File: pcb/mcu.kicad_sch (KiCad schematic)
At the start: 25 parts, among them J6 TC2030, U1 RP2040, U148 W25Q128JVS, Y1 ABM8AIG-12.000MHZ-12-2Z-T3

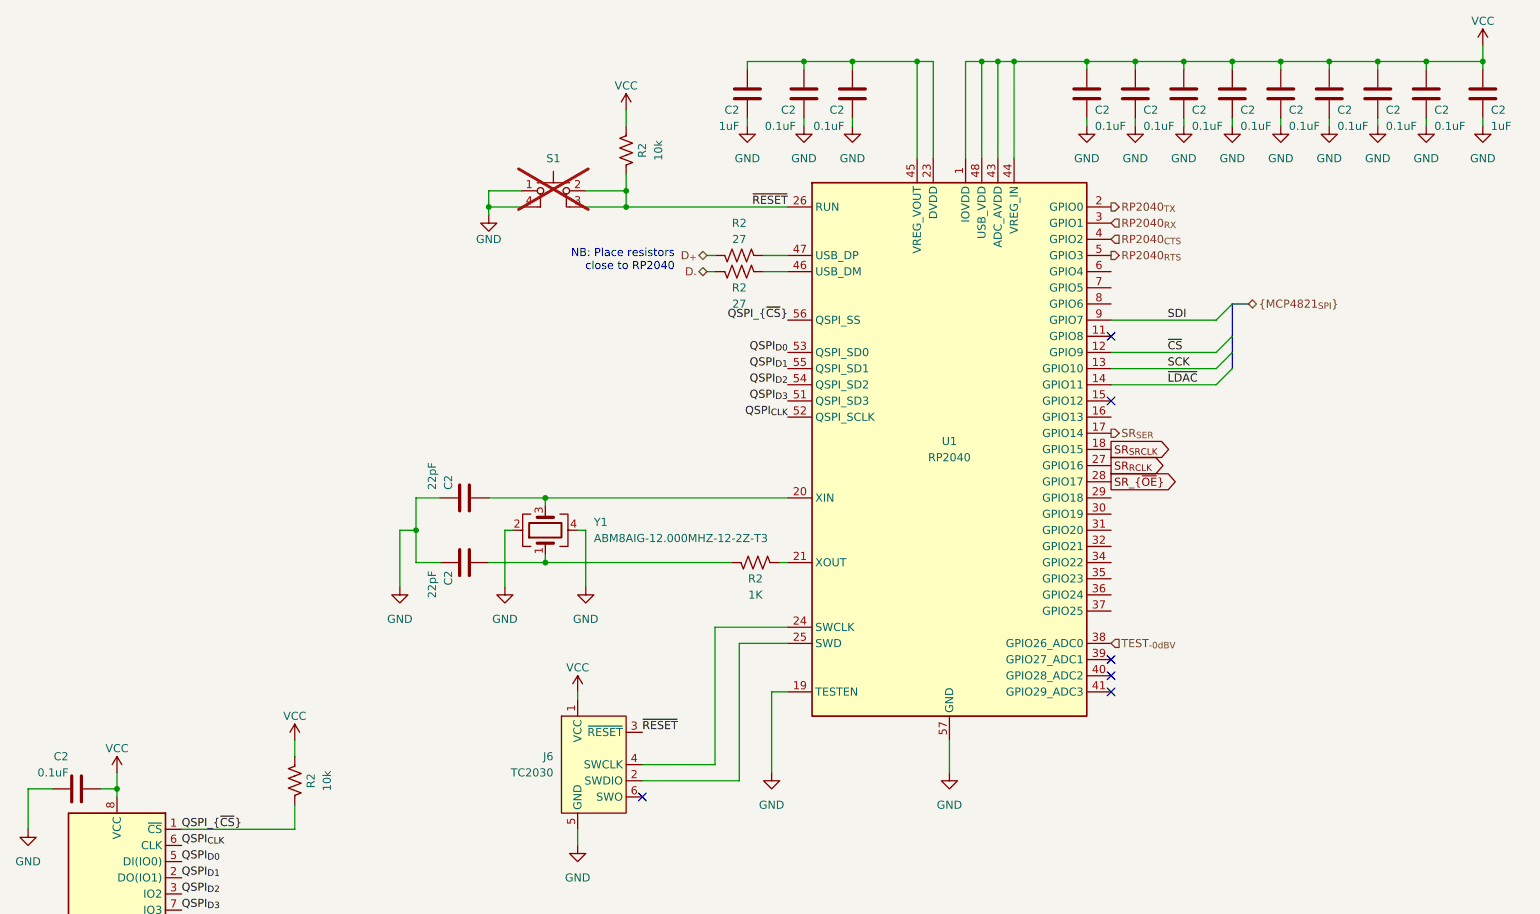
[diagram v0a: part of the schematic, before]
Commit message: Remove battery power option
- This device needs user IO
- Battery power means there would need to be a touch screen or wireless
  connection. Too complex.
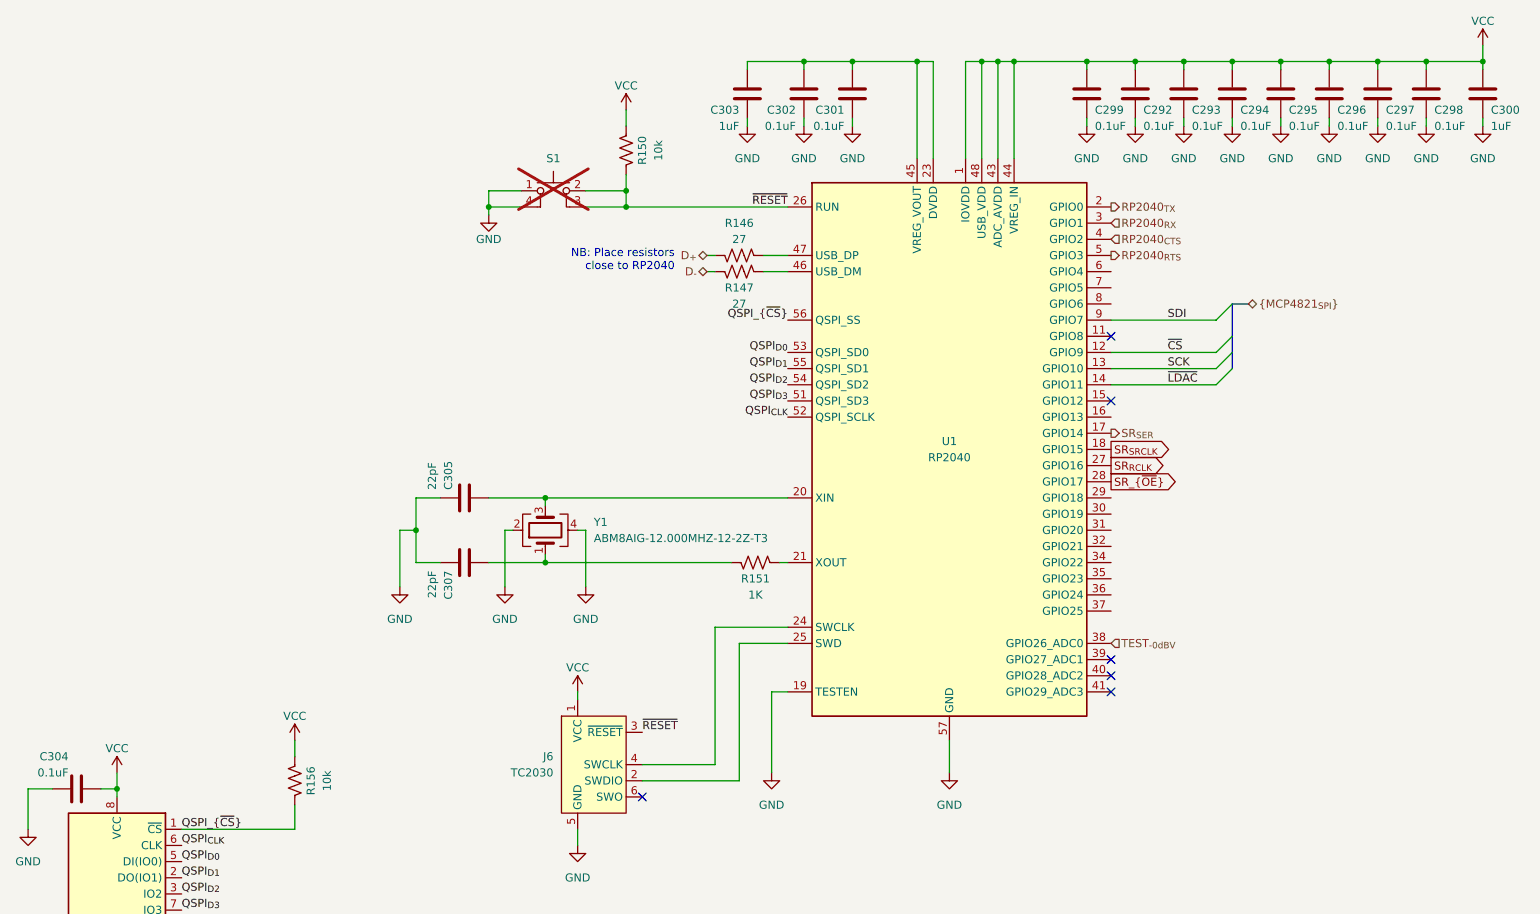
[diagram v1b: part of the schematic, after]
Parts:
- R146, R147, R150, R151, R156: renamed from R2; footprint (none) -> Resistor_SMD:R_0402_1005Metric
- S1: footprint (none) -> Button_Switch_THT:SW_PUSH_6mm_H4.3mm
- renumbered C2 to C292, C2 to C293, C2 to C294, C2 to C295, C2 to C296, C2 to C297, C2 to C298, C2 to C299, C2 to C300, C2 to C301, C2 to C302, C2 to C303, C2 to C304, C2 to C305, C2 to C307

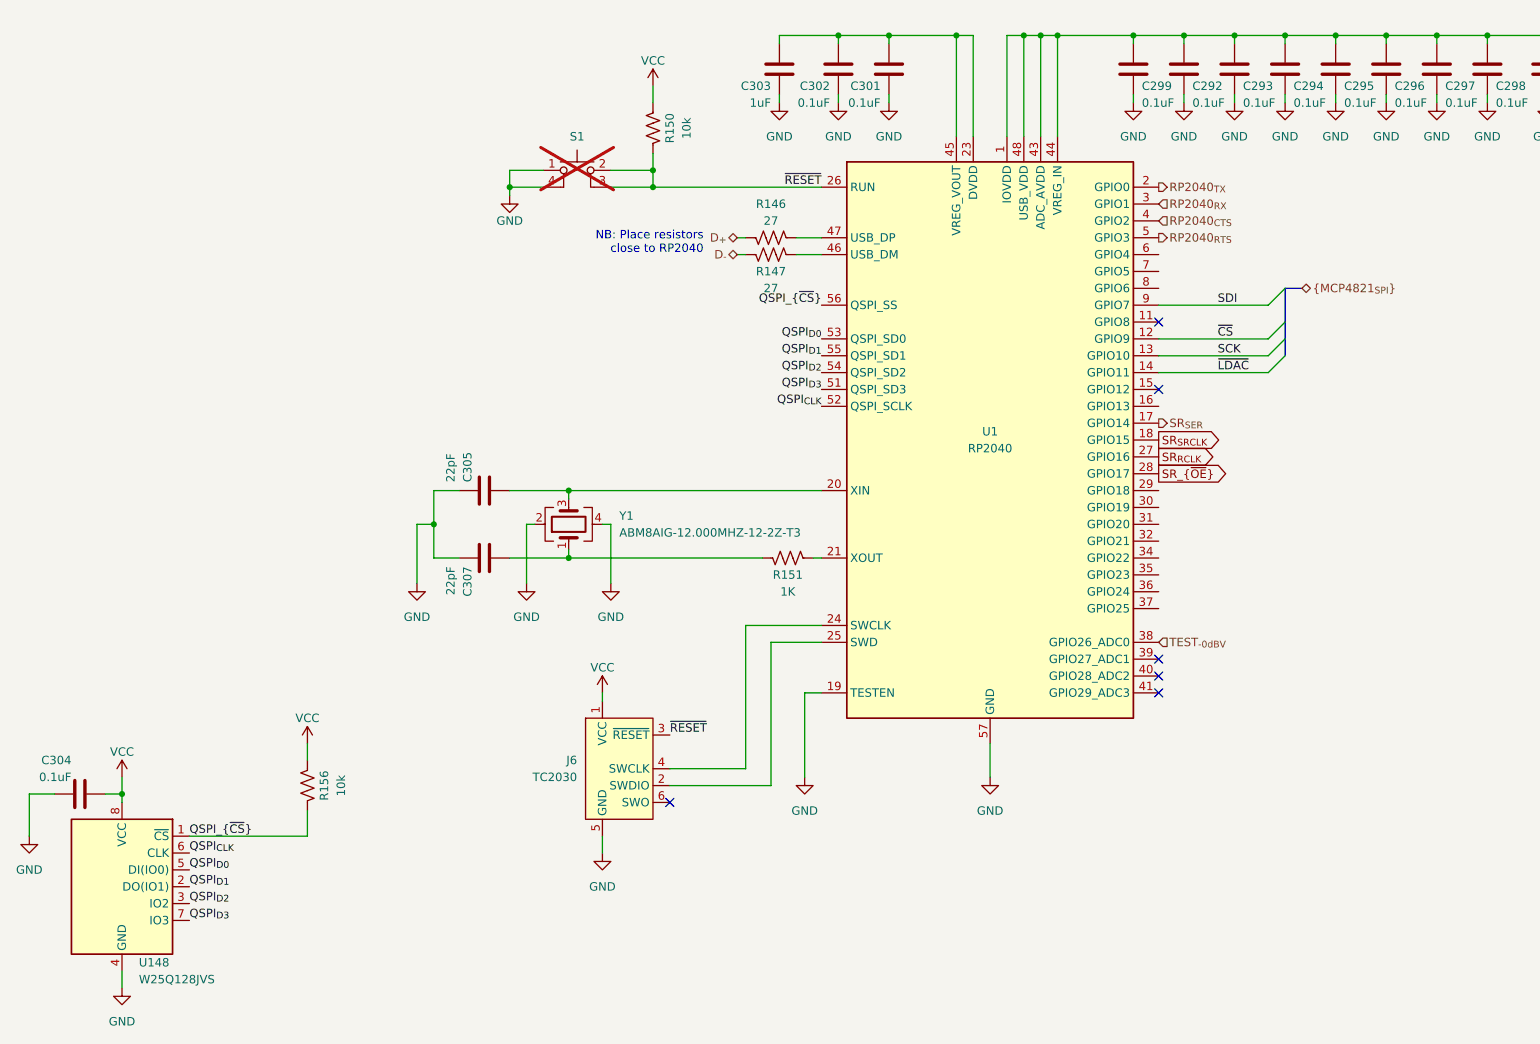
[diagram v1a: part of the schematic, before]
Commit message: Finished schematic, started routing
- There is a 8-channel motif that will need to be copied 16x on the
  board. I'm not sure the most efficient way to do this.
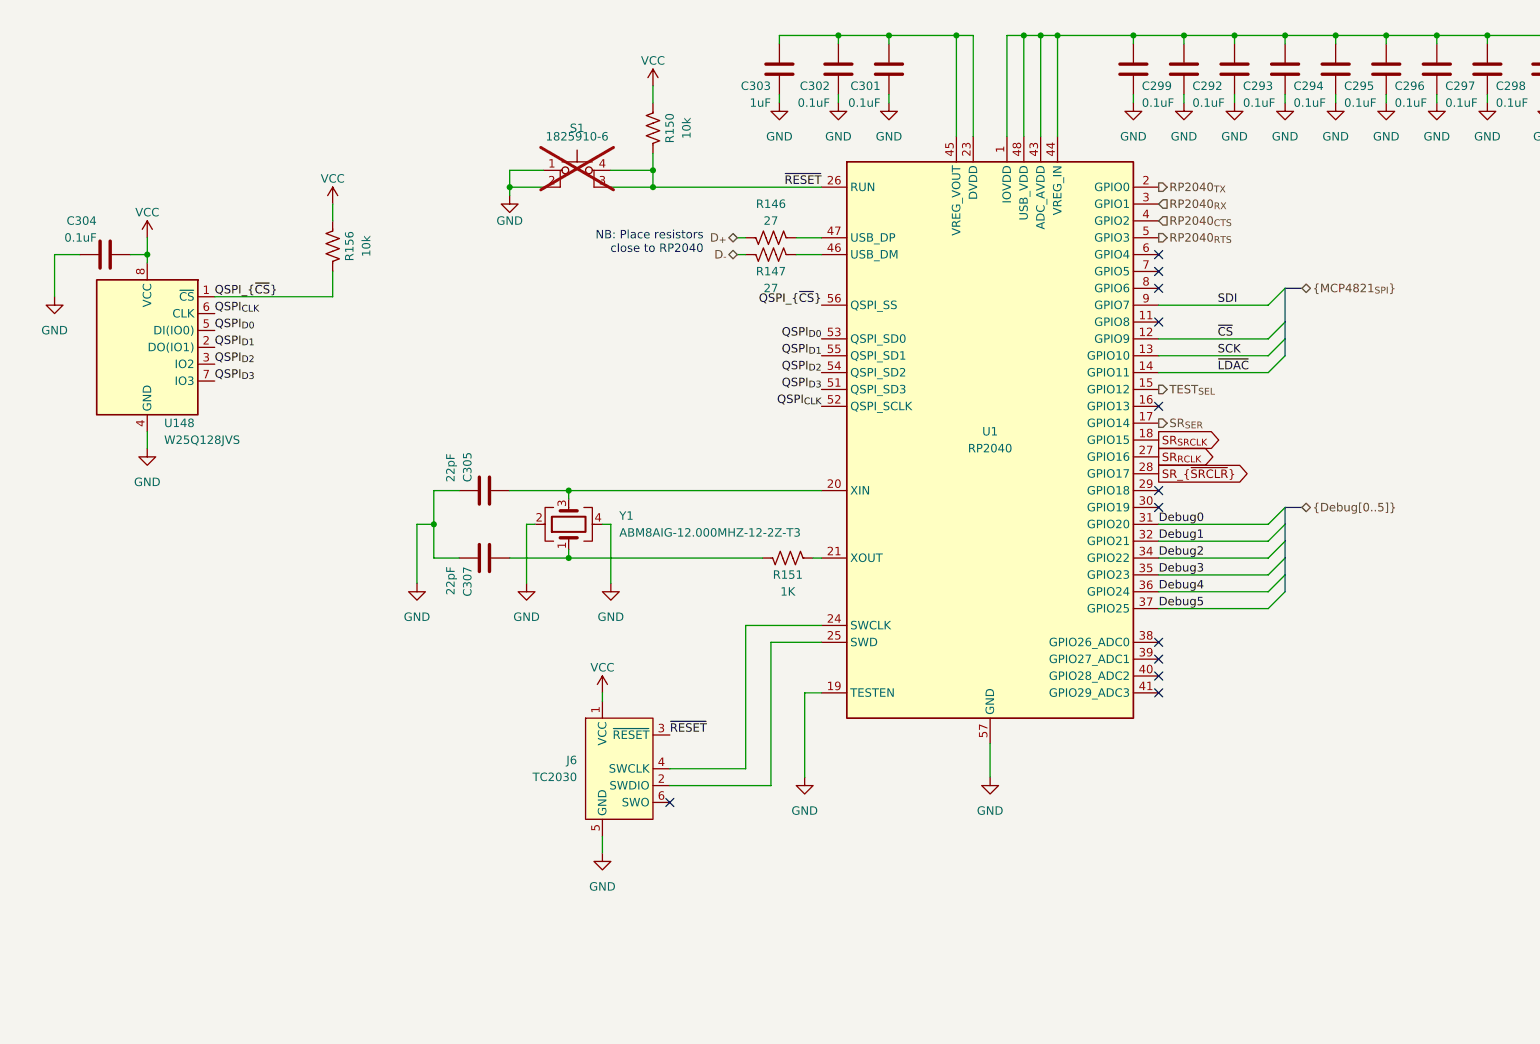
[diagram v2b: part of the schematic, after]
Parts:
- removed S1: ~, Button_Switch_THT:SW_PUSH_6mm_H4.3mm, symbol open-ephys:SW_TACT
- added S1: 1825910-6, Button_Switch_THT:SW_PUSH_6mm_H4.3mm, symbol Switch:SW_MEC_5E
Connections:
- net GND: now also S1.1, S1.2
- net ~{RESET}: now also S1.3 (K), S1.4 (A)
- net TEST_{SEL}: now reaches U1.15 (GPIO12)
- net Debug0: now reaches U1.31 (GPIO20)
- net Debug1: now reaches U1.32 (GPIO21)
- net Debug2: now reaches U1.34 (GPIO22)
- net Debug3: now reaches U1.35 (GPIO23)
- net Debug4: now reaches U1.36 (GPIO24)
- net Debug5: now reaches U1.37 (GPIO25)
- net SR_{~{OE}} renamed SR_{~{SRCLR}}
- net TEST_{-0dBV}: no longer names the net of U1.38 (GPIO26_ADC0)
- no-connect marks 6 -> 12
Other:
- moved on the sheet: C304, R156, U148

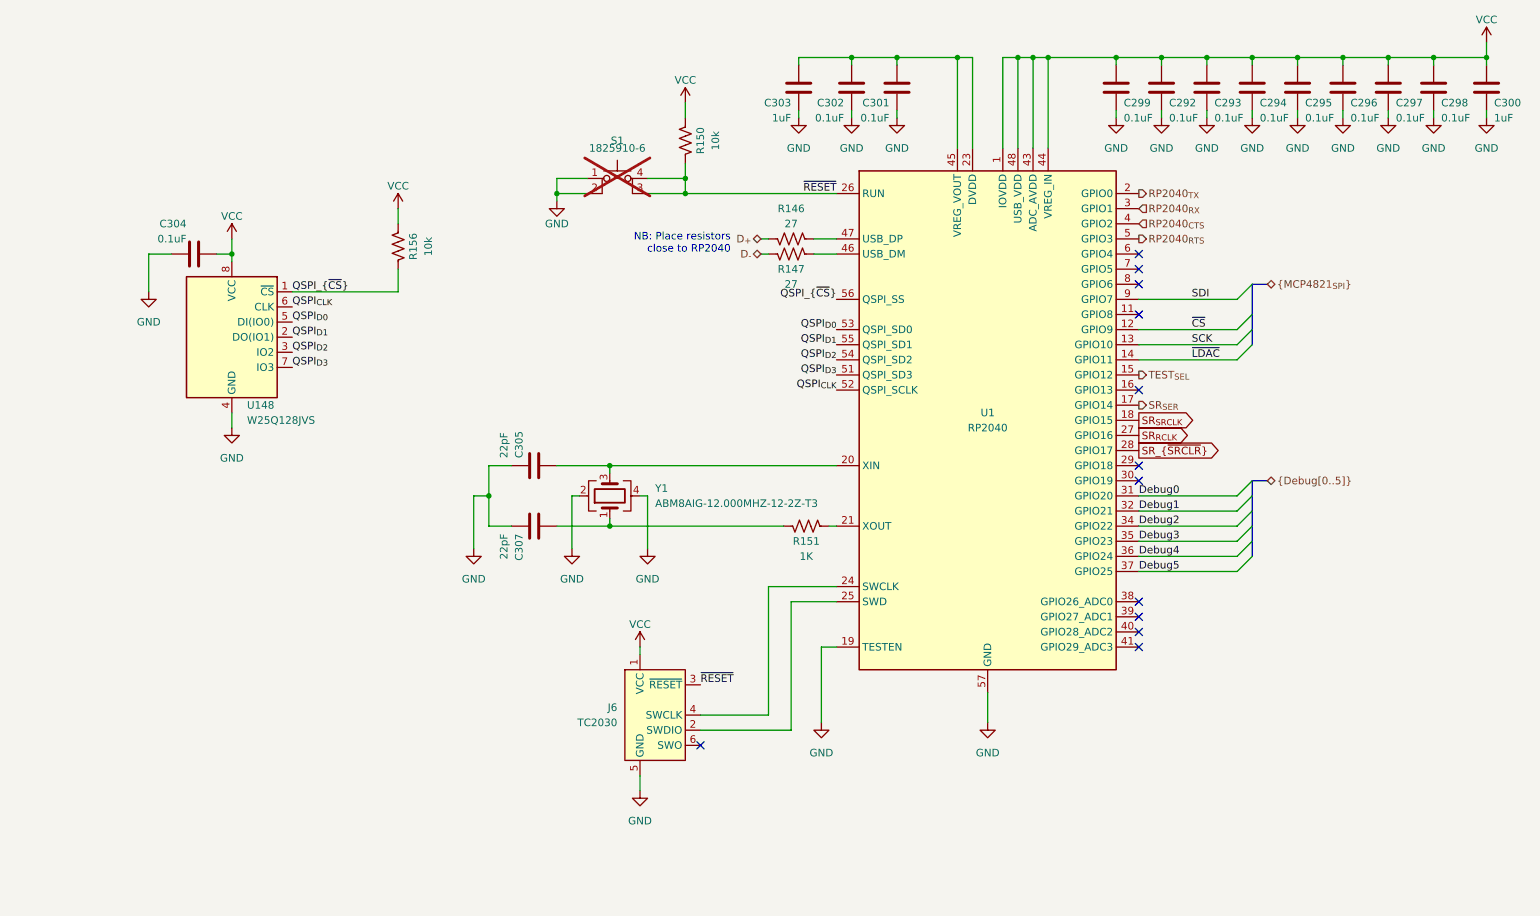
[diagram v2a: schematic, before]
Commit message: Motif is repeated
- some components are grouped by function
- components are roughly organized within groups
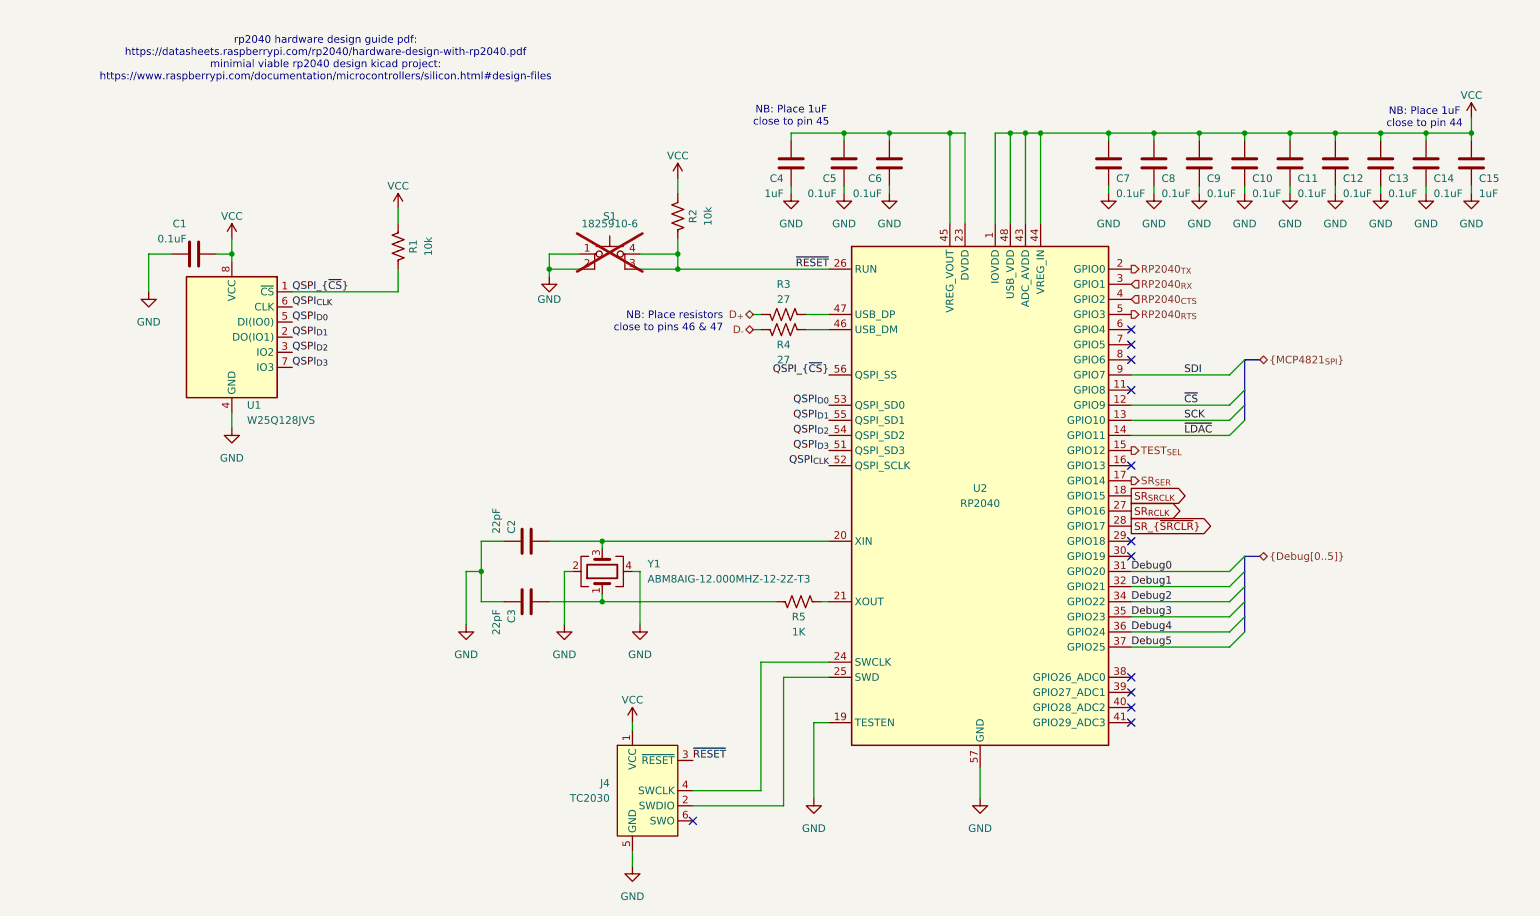
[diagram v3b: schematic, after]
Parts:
- renumbered C304 to C1, C294 to C10, C295 to C11, C296 to C12, C297 to C13, C298 to C14, C300 to C15, C305 to C2, C307 to C3, C303 to C4, C302 to C5, C301 to C6, C299 to C7, C292 to C8, C293 to C9, J6 to J4, R156 to R1, R150 to R2, R146 to R3, R147 to R4, R151 to R5, U148 to U1, U1 to U2
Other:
- note added: "NB: Place 1uF close to pin 44"
- note added: "NB: Place 1uF close to pin 45"
- note added: "NB: Place resistors close to pins 46 & 47"
- note added: "rp2040 hardware design guide pdf: https://datasheets.raspberrypi.com/rp2040/hardware-design-with-rp2040.pdf minimial viable rp2040 design kicad project: https://www.raspberrypi.com/documentation/microcontrollers/silicon.html#design-files"
- note removed: "NB: Place resistors close to RP2040"
- moved on the sheet: C10, C11, C12, C13, C14, C15, C2, C3, C4, C5, C6, C7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
